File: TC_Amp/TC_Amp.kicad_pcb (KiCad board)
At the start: 2 copper layers, 60 parts, among them J1 Screw_Terminal_01x02, J2 Screw_Terminal_01x02, J3 Conn_01x04_Pin, J4 Screw_Terminal_01x02, J5 Screw_Terminal_01x02, Q1 PMOS, U1 LT1025CN8-PBF, U10 LT1025CN8-PBF, U11 LM741, U12 LTC1049CN8_PBF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

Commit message: updated layout before traces
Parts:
- removed U1, U10, U6: LT1025CN8-PBF, Footprints:PDIP8_LT1025CN8-PBF_ADI
- added U15: LT1025CN8-PBF, Footprints:PDIP8_LT1025CN8-PBF_ADI, F.Cu at (27.3, 100.2)
- moved J3 145.8 mm to (125.5, 76.5)
- moved C8 124.9 mm to (46.5, 94.0)
- moved C7 124.8 mm to (40.5, 93.5)
- moved C11 121.9 mm to (53.2, 116.0)
- moved C10 118.8 mm to (53.2, 109.5)
- moved R17 111.7 mm to (52.6, 104.0)
- moved R16 103.4 mm to (52.5, 100.0)
- moved R20 94.9 mm to (79.2, 111.3)
- moved R10 94.8 mm to (40.3, 87.0)
- moved R9 94.3 mm to (40.3, 83.5)
- moved RV3 91.1 mm to (68.4, 101.5)
- moved R19 86.4 mm to (79.2, 119.3)
- moved R18 86.4 mm to (79.2, 115.3)
- moved R21 82.7 mm to (91.8, 105.8)
- moved C12 78.9 mm to (98.0, 100.0), turned to 180 degrees
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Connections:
- J4 pad 1: TC2_- -> TC1_-
- J5 pad 1: TC3_- -> TC1_-

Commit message: finished prelim traces
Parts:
- moved U15 55.8 mm to (61.2, 55.8), turned to 90 degrees
- moved J3 43.6 mm to (141.5, 36.0), turned to -90 degrees
- moved Q1 43.2 mm to (77.4, 37.8), turned to -90 degrees
- moved C13 42.8 mm to (83.8, 38.2), turned to 90 degrees
- moved C14 41.9 mm to (89.8, 50.8), turned to 0 degrees
- moved R19 41.9 mm to (119.3, 107.5)
- moved R18 41.7 mm to (119.3, 104.0)
- moved R20 41.6 mm to (119.3, 100.5)
- moved U13 41.3 mm to (140.8, 106.8)
- moved RV3 41.0 mm to (109.0, 95.5)
- moved RV1 40.9 mm to (109.0, 60.1)
- moved C12 40.9 mm to (138.5, 94.5)
- moved R23 40.9 mm to (93.8, 36.2), turned to -90 degrees
- moved C8 40.4 mm to (86.5, 88.5)
- moved C7 40.3 mm to (80.5, 88.5)
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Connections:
- J3 pad 1: TC1_OUT -> TC3_OUT
- J3 pad 3: TC3_OUT -> TC1_OUT
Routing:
- net -BATT: track 0.00 -> 323.1 mm
- net -5V: track 0.00 -> 269.5 mm, vias 0 -> 2
- net +5V: track 0.00 -> 266.4 mm
- net TC3_OUT: track 0.00 -> 83.2 mm
- net TC1_-: track 0.00 -> 72.9 mm
- net TC2_OUT: track 0.00 -> 66.4 mm
- net SIG1_AMPED: track 0.00 -> 61.6 mm
- net TC1_OUT: track 0.00 -> 49.1 mm
- net SIG3_AMPED: track 0.00 -> 44.1 mm
- net SIG2_AMPED: track 0.00 -> 40.7 mm, vias 0 -> 2
- net Net-(U8--IN): track 0.00 -> 28.1 mm
- net Net-(U5--IN): track 0.00 -> 27.6 mm
- net Net-(U9--IN): track 0.00 -> 27.2 mm
- net Net-(U2--IN): track 0.00 -> 27.1 mm
- net Net-(U13--IN): track 0.00 -> 27.0 mm
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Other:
- board outline added: 92 x 79.3 mm

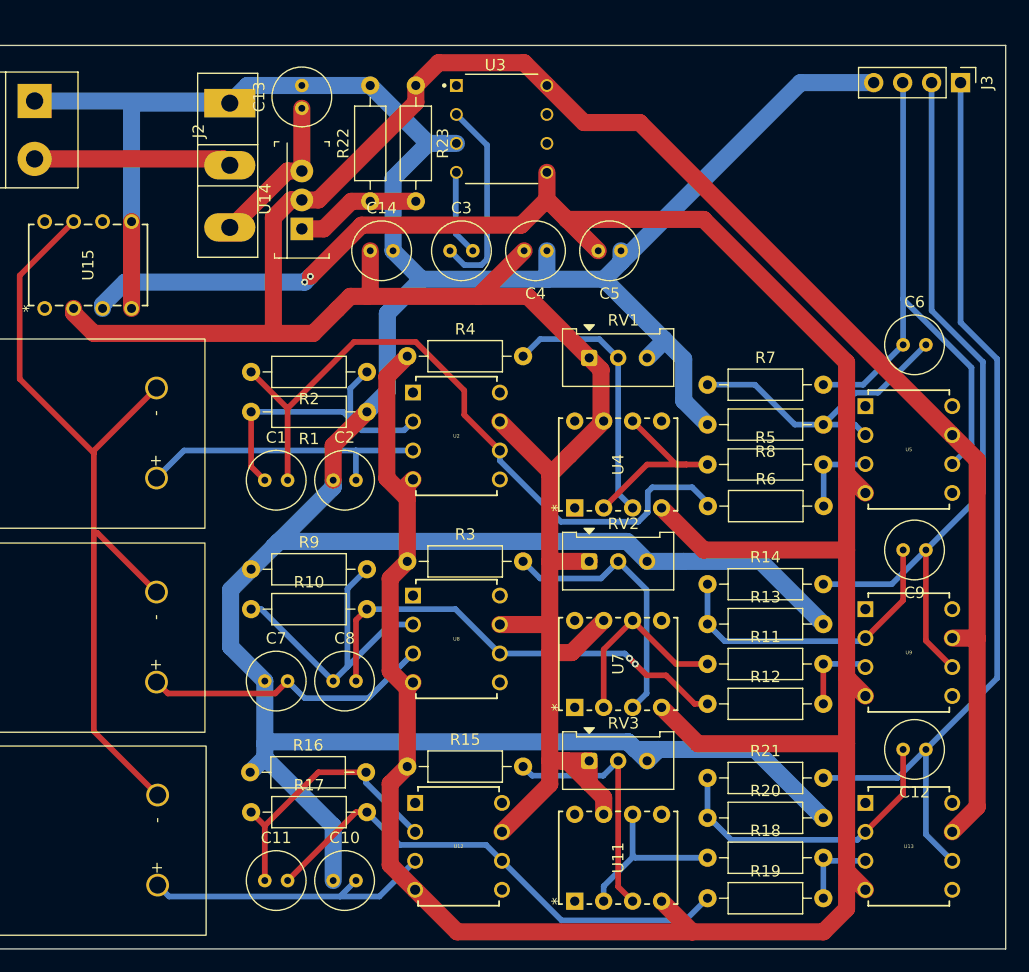
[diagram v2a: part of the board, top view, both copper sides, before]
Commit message: added silkscreen
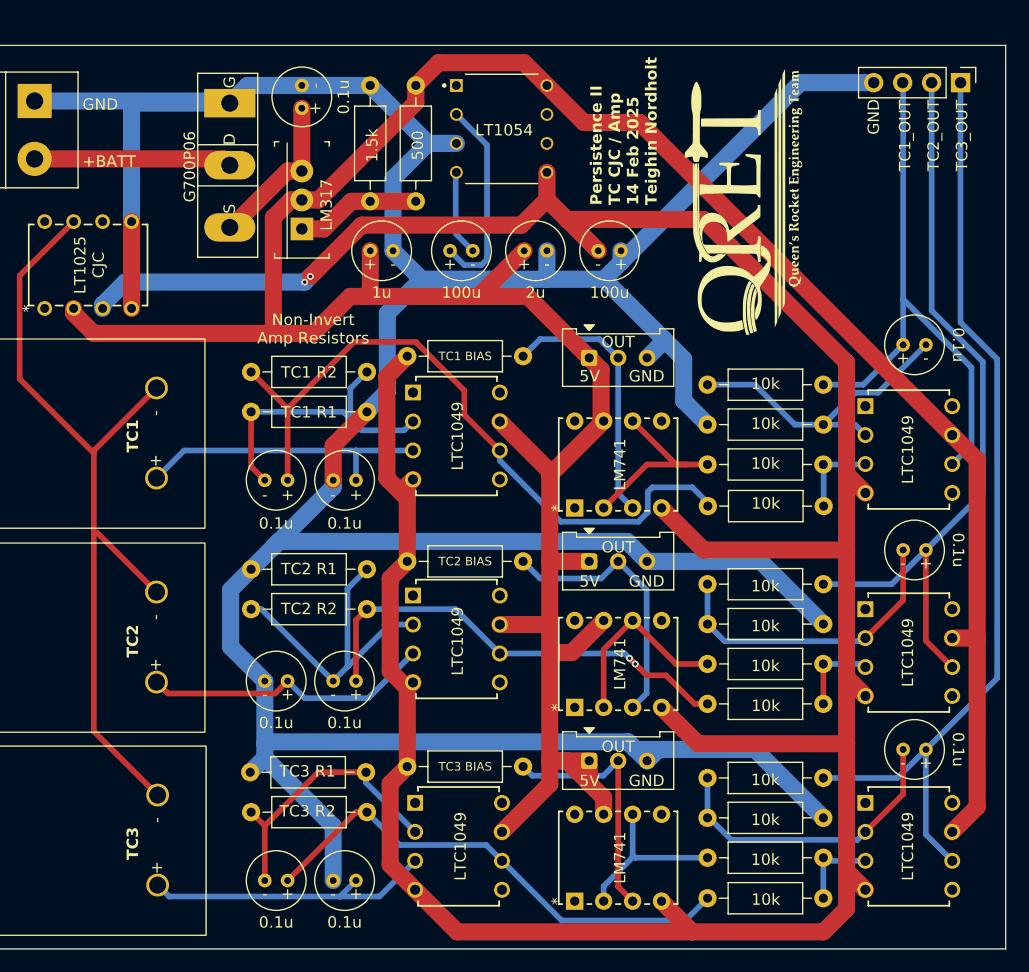
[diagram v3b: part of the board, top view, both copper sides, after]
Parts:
- added G***: LOGO, LOGO, F.Cu at (123.1, 47.3)
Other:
- board text added: "+"
- board text added: "+BATT"
- board text added: "-"
- board text added: "0.1u"
- board text added: "1.5k"
- board text added: "100u"
- board text added: "10k"
- board text added: "1u"
- board text added: "2u"
- board text added: "500"
- board text added: "5V"
- board text added: "D"
- board text added: "G"
- board text added: "G700P06"
- board text added: "GND"
- board text added: "LM317"
- board text added: "LM741"
- board text added: "LT1025 CJC"
- board text added: "LT1054"
- board text added: "LTC1049"
- board text added: "Non-Invert Amp Resistors"
- board text added: "OUT"
- board text added: "Persistence II TC CJC / Amp 14 Feb 2025 Teighin Nordholt"
- board text added: "S"
- board text added: "TC1"
- board text added: "TC1 BIAS"
- board text added: "TC1 R1"
- board text added: "TC1 R2"
- board text added: "TC1_OUT"
- board text added: "TC2"
- board text added: "TC2 BIAS"
- board text added: "TC2 R1"
- board text added: "TC2 R2"
- board text added: "TC2_OUT"
- board text added: "TC3"
- board text added: "TC3 BIAS"
- board text added: "TC3 R1"
- board text added: "TC3 R2"
- board text added: "TC3_OUT"

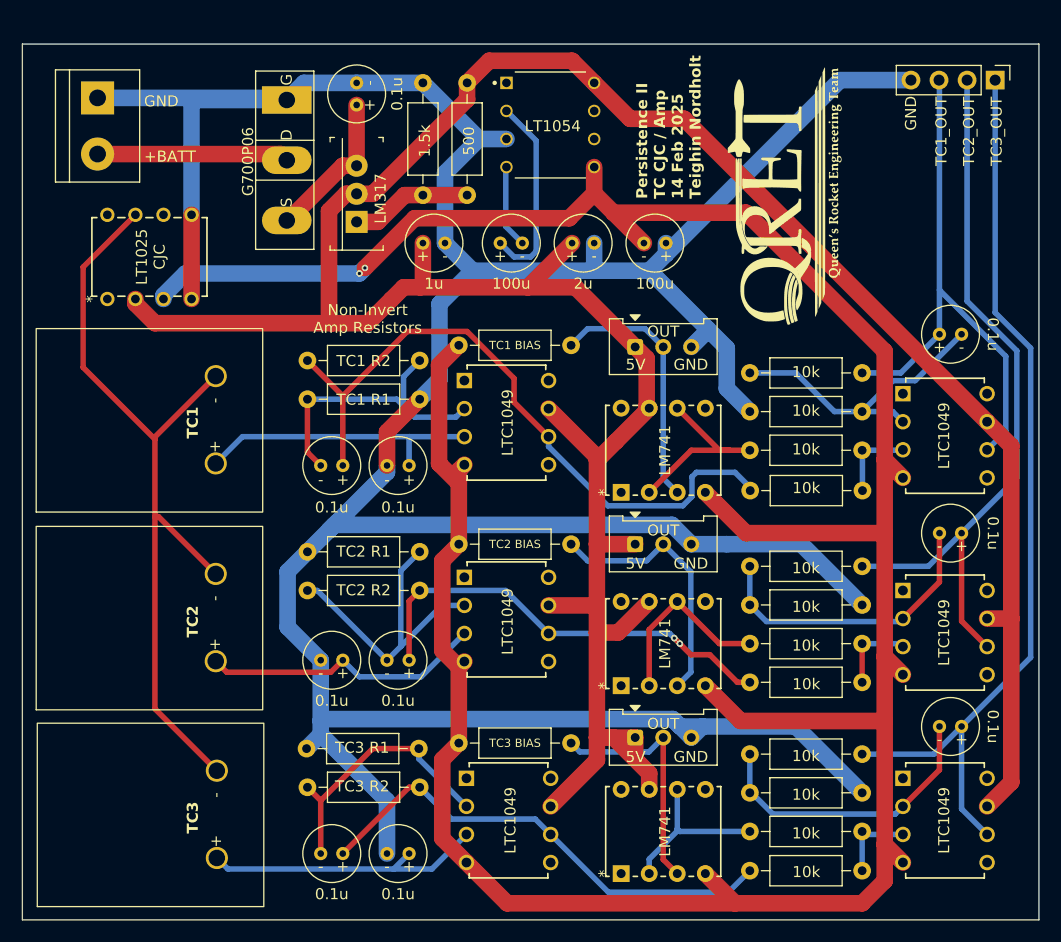
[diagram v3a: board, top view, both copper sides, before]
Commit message: rounded etch corners and added m3 holes
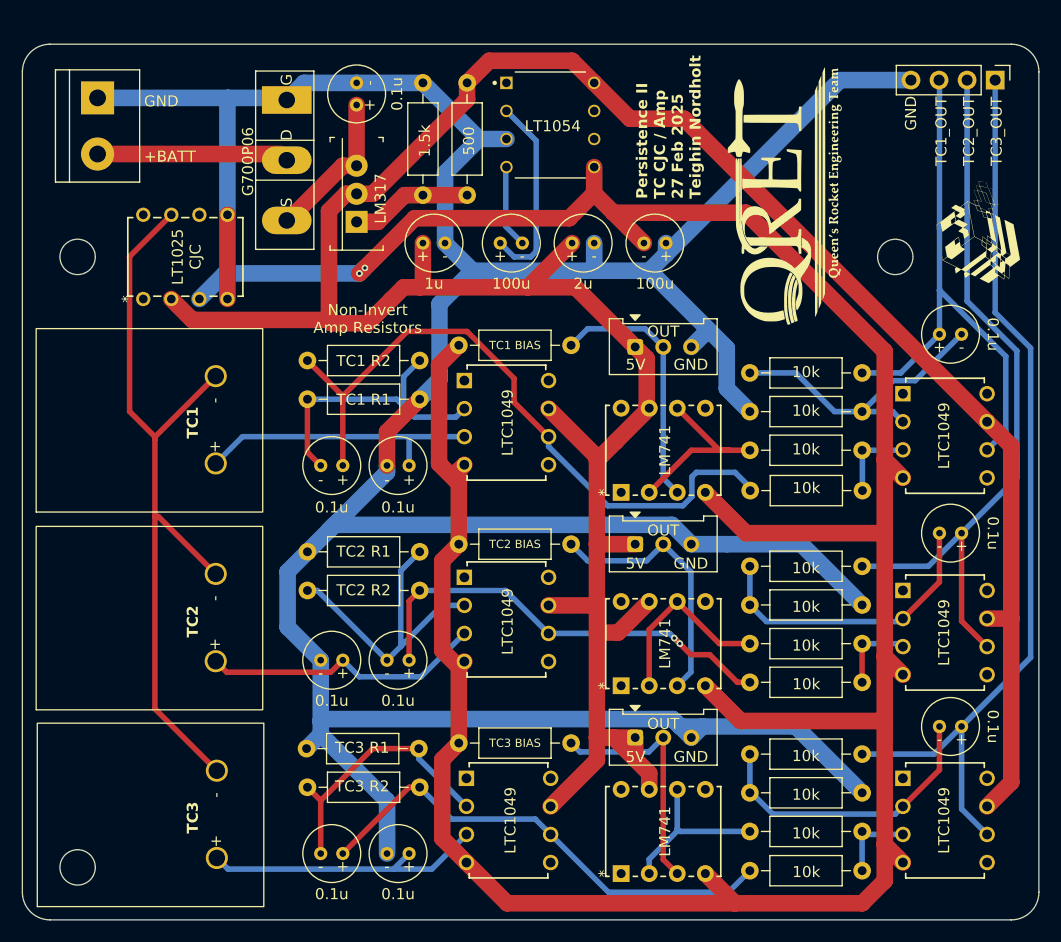
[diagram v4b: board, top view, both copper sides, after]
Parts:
- added G***: LOGO, LOGO, F.Cu at (140.3, 50.4)
- added H1: MountingHole, MountingHole:MountingHole_3.2mm_M3_DIN965, F.Cu at (58.5, 52.0)
- added H2: MountingHole, MountingHole:MountingHole_3.2mm_M3_DIN965, F.Cu at (132.5, 52.0)
- added H3: MountingHole, MountingHole:MountingHole_3.2mm_M3_DIN965, F.Cu at (58.5, 107.2)
- moved U15 3.25 mm to (64.4, 55.8)
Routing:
- net -BATT: track 323.1 -> 314.7 mm
- net +5V: track 266.4 -> 262.9 mm
- net -5V: track 269.5 -> 266.8 mm
- net TC1_-: track 72.9 -> 70.6 mm
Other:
- board size 92 x 79.3 mm -> 92 x 79.2 mm
- board text added: "Persistence II TC CJC / Amp 27 Feb 2025 Teighin Nordholt"
- board text removed: "Persistence II TC CJC / Amp 14 Feb 2025 Teighin Nordholt"
